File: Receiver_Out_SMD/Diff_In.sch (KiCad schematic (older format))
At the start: 7 parts, among them J7 RJ45, U3 AM26C32IN

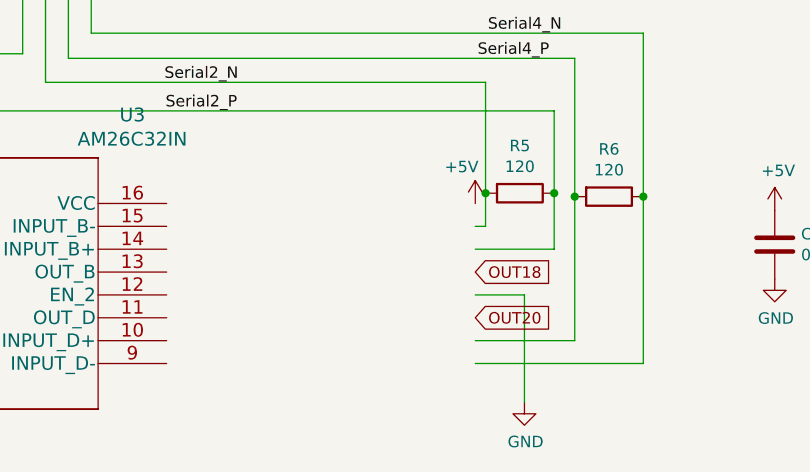
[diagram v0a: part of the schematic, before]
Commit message: added 24pin
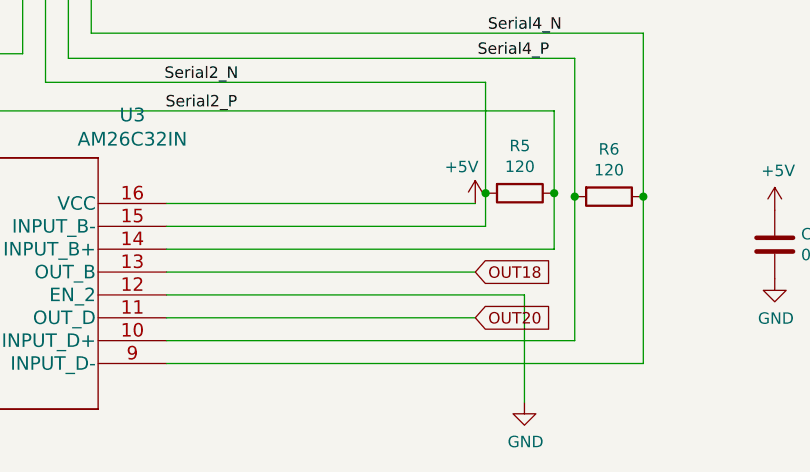
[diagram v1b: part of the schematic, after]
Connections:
- wire segments 44 -> 47
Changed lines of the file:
@@
 Connection ~ 4330 4860
 Wire Wire Line
-	7455 4560 7670 4560
-Wire Wire Line
 	7670 4560 7670 5030
 Wire Wire Line
@@
 	7800 3755 7800 4115
 Wire Wire Line
-	7800 4360 7455 4360
-Wire Wire Line
-	7455 4260 7500 4260
-Wire Wire Line
 	4455 4660 4060 4660
 Wire Wire Line
@@
 Wire Wire Line
 	7890 3525 7890 4130
-Wire Wire Line
-	7890 4760 7455 4760
-Wire Wire Line
-	7455 4860 8190 4860
 Wire Wire Line
 	8190 4860 8190 4130
@@
 Wire Wire Line
 	8190 4130 8190 3415
+Wire Wire Line
+	6105 4160 7455 4160
+Wire Wire Line
+	6105 4260 7500 4260
+Wire Wire Line
+	6105 4360 7800 4360
+Wire Wire Line
+	6105 4460 7455 4460
+Wire Wire Line
+	6105 4560 7670 4560
+Wire Wire Line
+	6105 4660 7455 4660
+Wire Wire Line
+	6105 4760 7890 4760
+Wire Wire Line
+	6105 4860 8190 4860
 $EndSCHEMATC
